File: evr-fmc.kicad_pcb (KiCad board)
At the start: 6 copper layers, 84 x 70.4 mm, 211 parts, among them J1 MMCX, J10 MMCX, J11 MMCX, J12 MMCX, J13 MMCX, J14 MMCX, J15 MMCX, J16 MMCX, J17 MMCX, J18 MMCX, J19 WP Jumper, J2 MMCX, J20 MMCX, J21 MMCX, J3 MMCX, J4 MMCX, J5 MMCX, J6 MMCX, J7 MMCX, J8 MMCX, J9 MMCX, P1 ASP-134488-01, Q1 FDN335N, Q2 FDN335N, T1 TCM2-43X, T2 TCM2-43X, T3 TCM2-43X, T4 TCM2-43X, U1 SN74LVC3G34DCT, U10 SN74LVC3G34DCT, U11 SN74LVC3G34DCT, U12 SN74LVC3G34DCT, U13 SN74LVC3G34DCT, U14 SN74LVC3G34DCT, U15 SN74LVC3G34DCT, U16 SN74LVC3G34DCT, U17 SN74LVC3G34DCT, U18 SI5394, U19 SI5394, U2 SN74LVC3G34DCT, U20 TLV75733PDBV, U21 TLV75718PDBV, U22 TPS562200, U23 74AVC4T245, U25 74AVC4T245, U26 74LVC8T245, U27 74LVC8T245, U3 SN74LVC3G34DCT, U4 SN74LVC3G34DCT, U5 SN74LVC3G34DCT, U6 SN74LVC3G34DCT, U7 SN74LVC3G34DCT, U8 SN74LVC3G34DCT, U9 AT24C64D, Y1 CX3225SB48000D0FPJC1, Y2 CX3225SB48000D0FPJC1

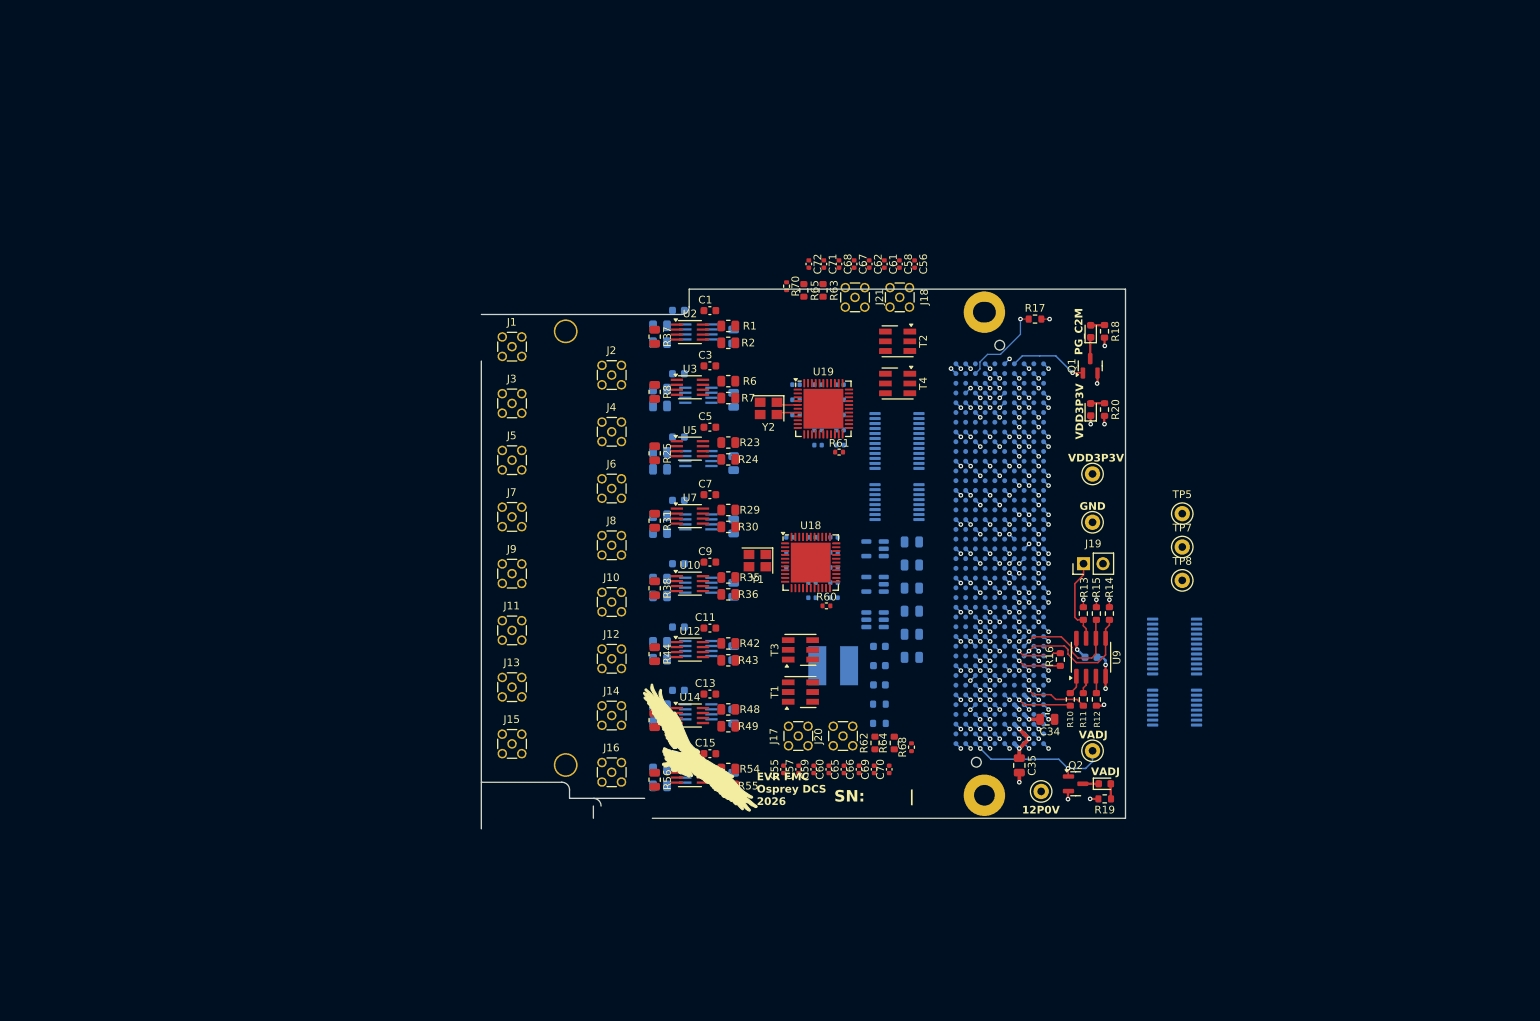
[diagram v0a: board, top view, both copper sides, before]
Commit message: Completed Schematic
Completed Schematic Draft
- Includes careful pin mapping to avoid conflicts with other firmwares
- Roughed out LCB layout high speed traces, and FMC breakouts.

Layout and BOM are still WIP
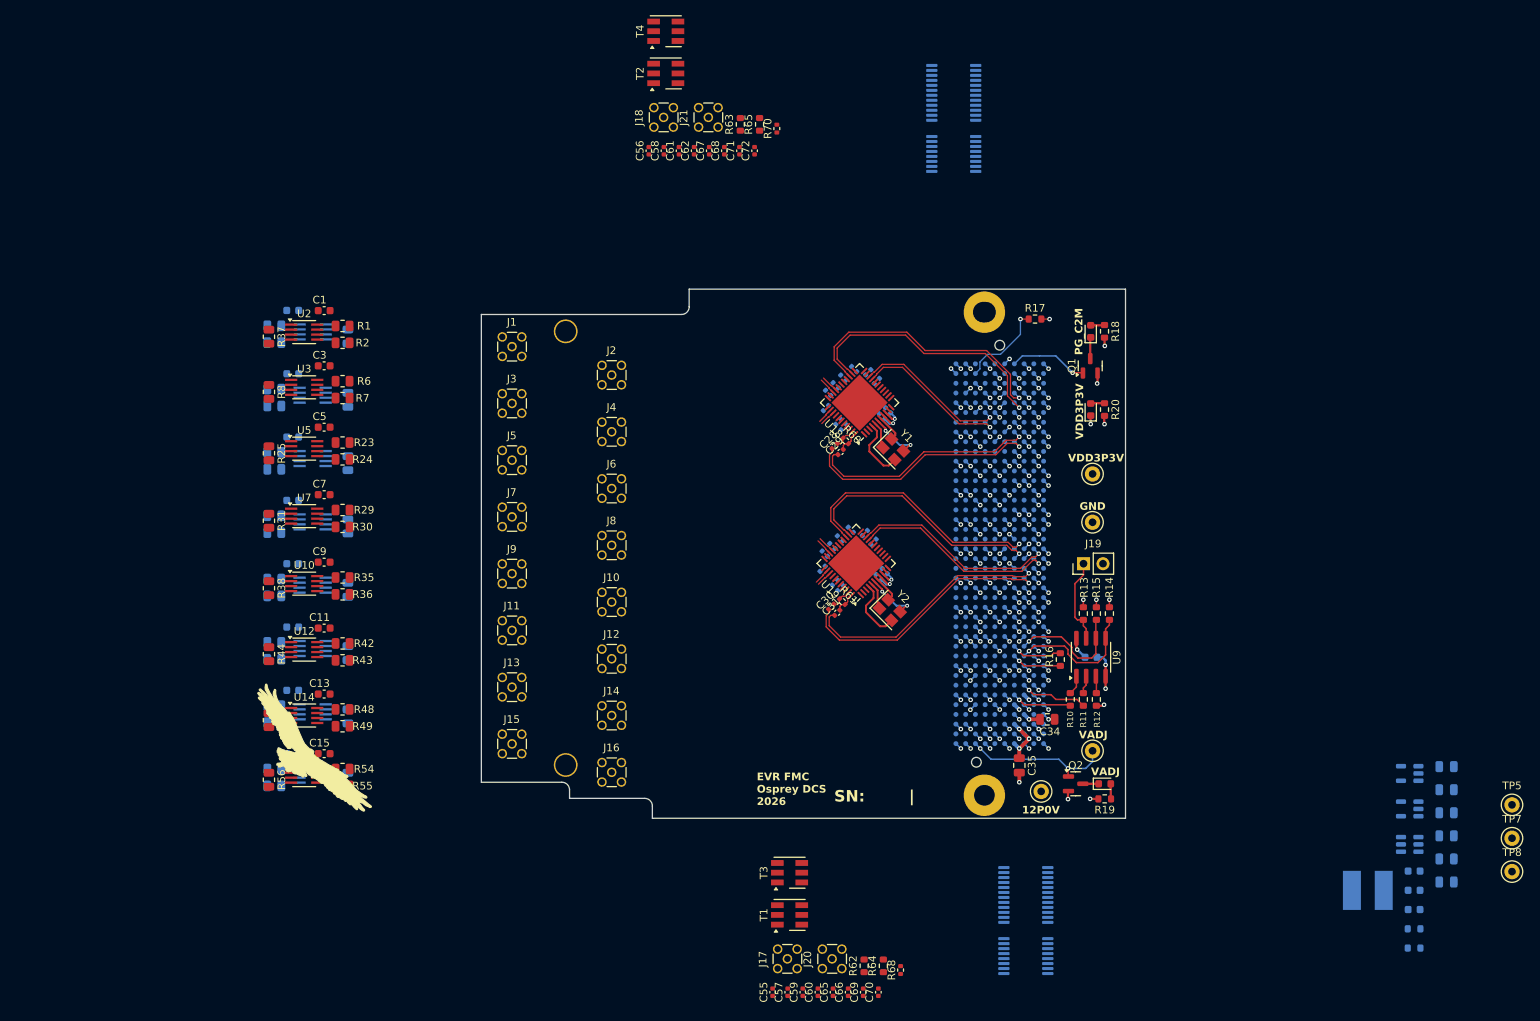
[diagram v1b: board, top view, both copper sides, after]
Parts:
- C28, C29, C30, C31: moved to F.Cu
- moved C48 75.6 mm to (232.9, 133.3)
- moved C49 75.6 mm to (232.9, 136.3)
- moved C50 75.6 mm to (232.9, 139.3)
- moved C51 75.6 mm to (232.9, 142.3)
- moved C53 75.6 mm to (232.9, 145.3)
- moved C54 75.6 mm to (232.9, 148.3)
- moved C46 75.6 mm to (228.6, 146.9)
- moved C47 75.6 mm to (228.6, 149.4)
- moved C52 75.6 mm to (228.6, 151.9)
- moved L1 75.6 mm to (222.6, 149.4)
- moved R66 75.6 mm to (228.6, 154.4)
- moved R67 75.6 mm to (228.6, 156.9)
- moved U20 75.6 mm to (228.1, 134.2)
- moved U21 75.6 mm to (228.1, 138.8)
- moved U22 75.6 mm to (228.1, 143.4)
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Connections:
- net Net-(U18-In0) renamed /Jitter Cleaner0/In0.P
- net Net-(U18-~{IN0}) renamed /Jitter Cleaner0/In0.N
- net Net-(U19-In0) renamed /Jitter Cleaner1/In0.P
- net Net-(U19-~{IN0}) renamed /Jitter Cleaner1/In0.N
- net P1_12P0V renamed +12V_FMC
- C28 pad 1: /FMC/FMC_CC_PAIR_0.P -> /FMC/Recovered_CLK_0.P
- C29 pad 1: /FMC/FMC_CC_PAIR_0.N -> /FMC/Recovered_CLK_0.N
- C30 pad 1: /FMC/FMC_CC_PAIR_1.P -> /FMC/Recovered_CLK_1.P
- C31 pad 1: /FMC/FMC_CC_PAIR_1.N -> /FMC/Recovered_CLK_1.N
- C47 pad 1: /Jitter Cleaner0/VDDA -> /Power/3P3V
- P1 pad C10: unconnected-(P1-PadC10) -> /FMC/Cleaner_SPI_0.CS
- P1 pad C11: unconnected-(P1-PadC11) -> /FMC/Cleaner_~{RST}_0
- P1 pad C14: unconnected-(P1-PadC14) -> /Digital IO/D_Output4
- P1 pad C15: unconnected-(P1-PadC15) -> /Digital IO/D_Output5
- P1 pad C18: unconnected-(P1-PadC18) -> /Digital IO/D_Output10
- P1 pad C19: unconnected-(P1-PadC19) -> /Digital IO/D_Output11
- P1 pad C22: unconnected-(P1-PadC22) -> /FMC/Recovered_CLK_1.N
- P1 pad C23: unconnected-(P1-PadC23) -> /FMC/Recovered_CLK_1.P
- P1 pad D12: unconnected-(P1-PadD12) -> /FMC/Cleaner_SPI_0.CLK
- P1 pad D14: unconnected-(P1-PadD14) -> /Digital IO/D_Output2
- P1 pad D15: unconnected-(P1-PadD15) -> /Digital IO/D_Output3
- P1 pad D17: unconnected-(P1-PadD17) -> /Digital IO/D_Output8
- P1 pad D18: unconnected-(P1-PadD18) -> /Digital IO/D_Output9
- P1 pad D20: unconnected-(P1-PadD20) -> /FMC/Cleaned_CLK_1.P
- P1 pad D21: unconnected-(P1-PadD21) -> /FMC/Cleaned_CLK_1.N
- P1 pad D24: unconnected-(P1-PadD24) -> /FMC/Cleaner_SPI_1.CLK
- P1 pad D26: unconnected-(P1-PadD26) -> /FMC/Cleaner_SPI_1.CS
- P1 pad D27: unconnected-(P1-PadD27) -> /FMC/Cleaner_~{RST}_1
- P1 pad D8: unconnected-(P1-PadD8) -> /FMC/Recovered_CLK_0.N
- P1 pad D9: unconnected-(P1-PadD9) -> /FMC/Recovered_CLK_0.P
- P1 pad G10: unconnected-(P1-PadG10) -> /FMC/Cleaner_SPI_0.DIN
- P1 pad G12: unconnected-(P1-PadG12) -> /Digital IO/D_Output0
- P1 pad G13: unconnected-(P1-PadG13) -> /Digital IO/D_Output1
- P1 pad G15: unconnected-(P1-PadG15) -> /Digital IO/D_Output6
- P1 pad G16: unconnected-(P1-PadG16) -> /Digital IO/D_Output7
- P1 pad G18: unconnected-(P1-PadG18) -> /Digital IO/D_Output12
- P1 pad G19: unconnected-(P1-PadG19) -> /Digital IO/D_Output13
- P1 pad G2: /FMC/FMC_CLK1_M2C.P -> unconnected-(P1-PadG2)
- P1 pad G21: unconnected-(P1-PadG21) -> /Digital IO/D_Output14
- P1 pad G22: unconnected-(P1-PadG22) -> /Digital IO/D_Output15
- P1 pad G24: unconnected-(P1-PadG24) -> /FMC/Cleaner_SPI_1.OE
- P1 pad G25: unconnected-(P1-PadG25) -> /FMC/Cleaner_SPI_1.DIN
- P1 pad G3: /FMC/FMC_CLK1_M2C.N -> unconnected-(P1-PadG3)
- P1 pad G6: unconnected-(P1-PadG6) -> /FMC/Cleaned_CLK_0.P
- P1 pad G7: unconnected-(P1-PadG7) -> /FMC/Cleaned_CLK_0.N
- P1 pad G9: unconnected-(P1-PadG9) -> /FMC/Cleaner_SPI_0.OE
- P1 pad H10: unconnected-(P1-PadH10) -> /FMC/Cleaner_Fault_0.LOL
- P1 pad H11: unconnected-(P1-PadH11) -> /FMC/Cleaner_SPI_0.DOUT
- P1 pad H25: unconnected-(P1-PadH25) -> /FMC/Cleaner_Fault_1.INTR
- P1 pad H26: unconnected-(P1-PadH26) -> /FMC/Cleaner_Fault_1.LOS_XO
- P1 pad H28: unconnected-(P1-PadH28) -> /FMC/Cleaner_Fault_1.LOL
- P1 pad H29: unconnected-(P1-PadH29) -> /FMC/Cleaner_SPI_1.DOUT
- P1 pad H4: /FMC/FMC_CLK0_M2C.P -> unconnected-(P1-PadH4)
- P1 pad H5: /FMC/FMC_CLK0_M2C.N -> unconnected-(P1-PadH5)
- P1 pad H7: unconnected-(P1-PadH7) -> /FMC/Cleaner_Fault_0.INTR
- P1 pad H8: unconnected-(P1-PadH8) -> /FMC/Cleaner_Fault_0.LOS_XO
- R10 pad 1: /EEPROM/GA1 -> /FMC/EEPROM_GA1
- R11 pad 1: /EEPROM/GA0 -> /FMC/EEPROM_GA0
- R14 pad 2: /EEPROM/SDA -> /FMC/EEPROM_SDA
- R15 pad 2: /EEPROM/SCL -> /FMC/EEPROM_SCL
- T1 pad 5: (no net) -> unconnected-(T1-OUT2-Pad5)
- T2 pad 5: (no net) -> unconnected-(T2-OUT2-Pad5)
- T3 pad 5: (no net) -> unconnected-(T3-OUT2-Pad5)
- T4 pad 5: (no net) -> unconnected-(T4-OUT2-Pad5)
- U18 pad 19: /FMC/FMC_GBTCLK0.N -> /FMC/Cleaned_CLK_0.N
- U18 pad 20: /FMC/FMC_GBTCLK0.P -> /FMC/Cleaned_CLK_0.P
- U18 pad 24: /FMC/FMC_CLK0_M2C.N -> /FMC/FMC_GBTCLK0.N
- U18 pad 25: /FMC/FMC_CLK0_M2C.P -> /FMC/FMC_GBTCLK0.P
- U19 pad 24: /FMC/FMC_CLK1_M2C.N -> /FMC/Cleaned_CLK_1.N
- U19 pad 25: /FMC/FMC_CLK1_M2C.P -> /FMC/Cleaned_CLK_1.P
- U21 pad 1: /Jitter Cleaner0/VDDA -> /Power/3P3V
- U21 pad 3: /Jitter Cleaner0/VDDA -> /Power/3P3V
- U23 pad 4: /Jitter Cleaner0/Cleaner_Fault.INTR -> /FMC/Cleaner_Fault_0.INTR
- U23 pad 5: /Jitter Cleaner0/Cleaner_Fault.LOS_XO -> /FMC/Cleaner_Fault_0.LOS_XO
- U23 pad 6: /Jitter Cleaner0/Cleaner_Fault.LOL -> /FMC/Cleaner_Fault_0.LOL
- U23 pad 7: /Jitter Cleaner0/Cleaner_SPI.DOUT -> /FMC/Cleaner_SPI_0.DOUT
- U25 pad 4: /Jitter Cleaner1/Cleaner_Fault.INTR -> /FMC/Cleaner_Fault_1.INTR
- U25 pad 5: /Jitter Cleaner1/Cleaner_Fault.LOS_XO -> /FMC/Cleaner_Fault_1.LOS_XO
- U25 pad 6: /Jitter Cleaner1/Cleaner_Fault.LOL -> /FMC/Cleaner_Fault_1.LOL
- U25 pad 7: /Jitter Cleaner1/Cleaner_SPI.DOUT -> /FMC/Cleaner_SPI_1.DOUT
- U26 pad 3: /Jitter Cleaner0/Cleaner_SPI.OE -> /FMC/Cleaner_SPI_0.OE
- U26 pad 4: /Jitter Cleaner0/Cleaner_SPI.DIN -> /FMC/Cleaner_SPI_0.DIN
- U26 pad 5: /Jitter Cleaner0/Cleaner_SPI.CLK -> /FMC/Cleaner_SPI_0.CLK
- U26 pad 7: /Jitter Cleaner0/Cleaner_SPI.CS -> /FMC/Cleaner_SPI_0.CS
- U26 pad 8: /Jitter Cleaner0/~{RST} -> /FMC/Cleaner_~{RST}_0
- U27 pad 3: /Jitter Cleaner1/Cleaner_SPI.OE -> /FMC/Cleaner_SPI_1.OE
- U27 pad 4: /Jitter Cleaner1/Cleaner_SPI.DIN -> /FMC/Cleaner_SPI_1.DIN
- U27 pad 5: /Jitter Cleaner1/Cleaner_SPI.CLK -> /FMC/Cleaner_SPI_1.CLK
- U27 pad 7: /Jitter Cleaner1/Cleaner_SPI.CS -> /FMC/Cleaner_SPI_1.CS
- U27 pad 8: /Jitter Cleaner1/~{RST} -> /FMC/Cleaner_~{RST}_1
- U9 pad 5: /EEPROM/SDA -> /FMC/EEPROM_SDA
- U9 pad 6: /EEPROM/SCL -> /FMC/EEPROM_SCL
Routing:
- net /FMC/FMC_GBTCLK0.P: track 0.91 -> 35.6 mm
- net /FMC/FMC_GBTCLK0.N: track 0.91 -> 35.0 mm
- net /FMC/Cleaned_CLK_1.P: track 0.00 -> 34.1 mm, vias 0 -> 1
- net /FMC/Recovered_CLK_1.P: track 0.00 -> 34.0 mm, vias 0 -> 1
- net /FMC/Cleaned_CLK_1.N: track 0.00 -> 33.1 mm, vias 0 -> 1
- net /FMC/Recovered_CLK_1.N: track 0.00 -> 33.1 mm, vias 0 -> 1
- net /FMC/Recovered_CLK_0.P: track 0.00 -> 30.9 mm, vias 0 -> 1
- net /FMC/Recovered_CLK_0.N: track 0.00 -> 29.9 mm, vias 0 -> 1
- net /FMC/FMC_GBTCLK1.P: track 0.91 -> 27.2 mm
- net /FMC/FMC_GBTCLK1.N: track 0.91 -> 26.9 mm
- net /FMC/Cleaned_CLK_0.P: track 0.00 -> 20.5 mm, vias 0 -> 1
- net /FMC/Cleaned_CLK_0.N: track 0.00 -> 20.2 mm, vias 0 -> 1
- net /Jitter Cleaner0/VDDA: track 0.00 -> 11.3 mm, vias 0 -> 4
- net Net-(U18-X1): track 0.00 -> 8.37 mm
- net Net-(U19-X1): track 0.00 -> 8.37 mm
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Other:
- board size 84 x 70.4 mm -> 84 x 69 mm

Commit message: Updated Schematic and continued layout work
schematic:
- Added 0ohm resistor in power section
- Added pull up and down to digital lines to define powerup behavior
- Added some power filter between jitter cleaner IC's

layout:
-Overall Still WIP
-defined all needed fmc pins
-started layout of critical clock signals and connector locations.
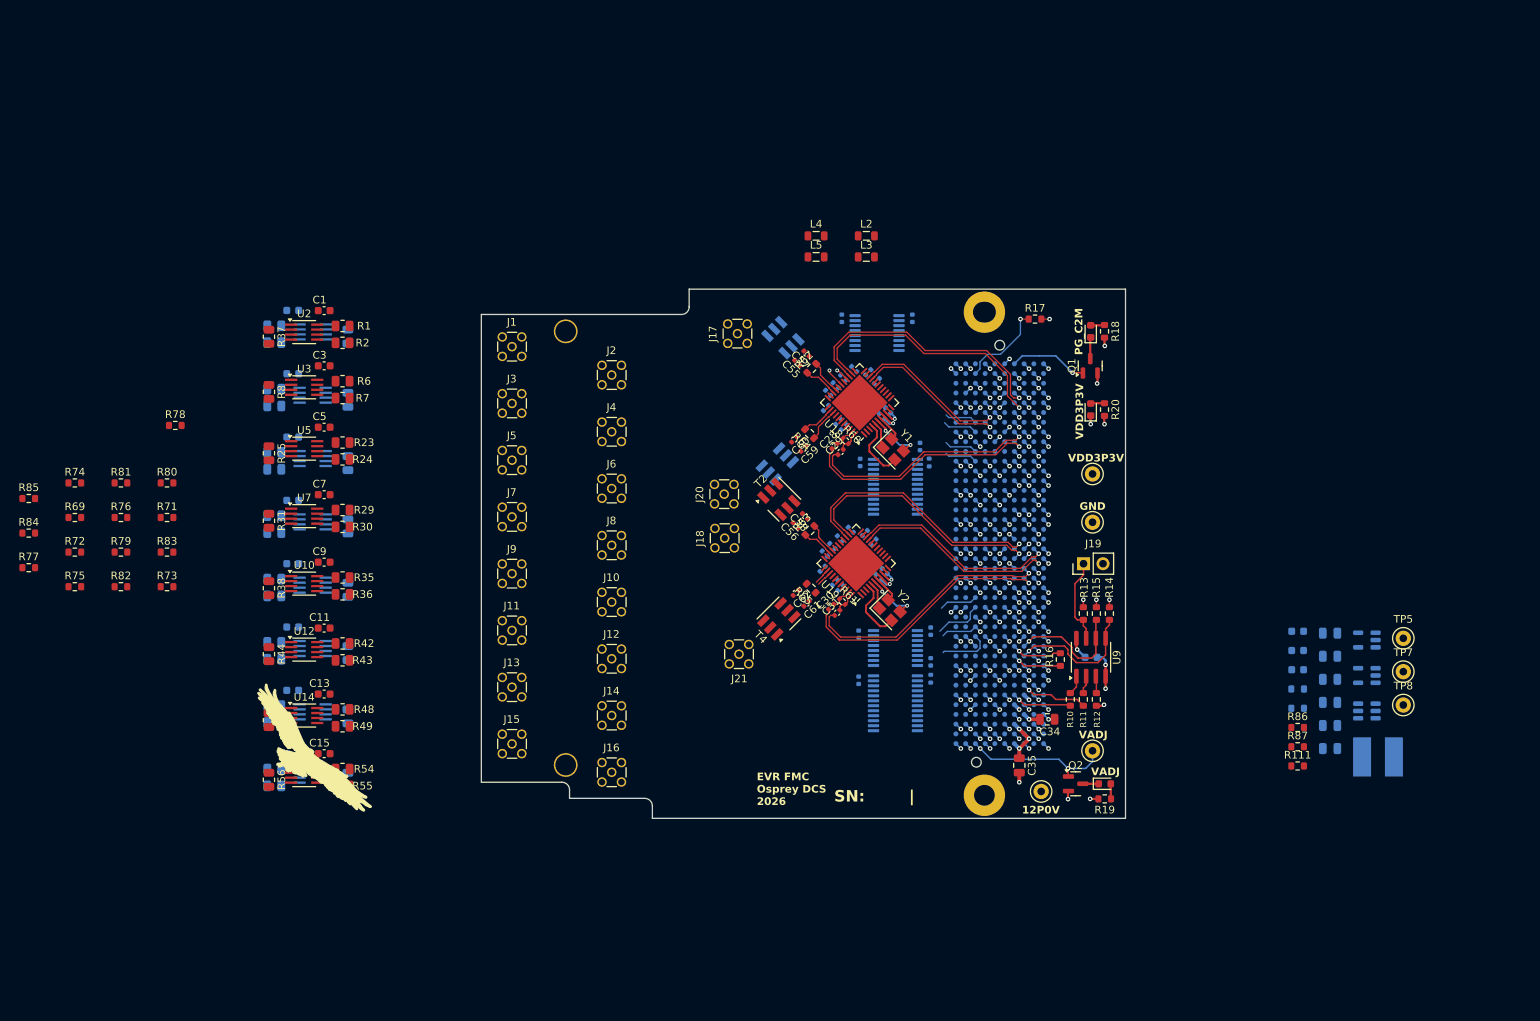
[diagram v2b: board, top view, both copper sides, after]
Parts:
- added L2: 60R@100Mhz; 3.5A, Inductor_SMD:L_0805_2012Metric, F.Cu at (157.2, 64.0)
- added L3: 60R@100Mhz; 3.5A, Inductor_SMD:L_0805_2012Metric, F.Cu at (157.2, 66.8)
- added L4: 60R@100Mhz; 3.5A, Inductor_SMD:L_0805_2012Metric, F.Cu at (150.7, 64.0)
- added L5: 60R@100Mhz; 3.5A, Inductor_SMD:L_0805_2012Metric, F.Cu at (150.7, 66.8)
- added R111: 0R, Resistor_SMD:R_0603_1608Metric, F.Cu at (213.4, 133.2)
- added R69: 11.5k, Resistor_SMD:R_0603_1608Metric, F.Cu at (54.0, 100.8)
- added R71: 11.5k, Resistor_SMD:R_0603_1608Metric, F.Cu at (66.0, 100.8)
- added R72: 11.5k, Resistor_SMD:R_0603_1608Metric, F.Cu at (54.0, 105.3)
- added R73: 11.5k, Resistor_SMD:R_0603_1608Metric, F.Cu at (66.0, 109.8)
- added R74: 11.5k, Resistor_SMD:R_0603_1608Metric, F.Cu at (54.0, 96.3)
- added R75: 11.5k, Resistor_SMD:R_0603_1608Metric, F.Cu at (54.0, 109.8)
- added R76: 11.5k, Resistor_SMD:R_0603_1608Metric, F.Cu at (60.0, 100.8)
- added R77: 11.5k, Resistor_SMD:R_0603_1608Metric, F.Cu at (48.0, 107.3)
- added R78: 11.5k, Resistor_SMD:R_0603_1608Metric, F.Cu at (67.1, 88.8)
- added R79: 11.5k, Resistor_SMD:R_0603_1608Metric, F.Cu at (60.0, 105.3)
- added R80: 11.5k, Resistor_SMD:R_0603_1608Metric, F.Cu at (66.0, 96.3)
- added R81: 11.5k, Resistor_SMD:R_0603_1608Metric, F.Cu at (60.0, 96.3)
- added R82: 11.5k, Resistor_SMD:R_0603_1608Metric, F.Cu at (60.0, 109.8)
- added R83: 11.5k, Resistor_SMD:R_0603_1608Metric, F.Cu at (66.0, 105.3)
- added R84: 11.5k, Resistor_SMD:R_0603_1608Metric, F.Cu at (48.0, 102.8)
- added R85: 11.5k, Resistor_SMD:R_0603_1608Metric, F.Cu at (48.0, 98.3)
- added R86: 0R, Resistor_SMD:R_0603_1608Metric, F.Cu at (213.4, 128.2)
- added R87: 0R, Resistor_SMD:R_0603_1608Metric, F.Cu at (213.4, 130.7)
- C65, C66, C67, C68, C69, C70, C71, C72, R68, R70: moved to B.Cu
- T1, T3: value TCM2-43X -> TCM2-43X+; moved to B.Cu
- T2, T4: value TCM2-43X -> TCM2-43X+
- moved C66 88.3 mm to (163.2, 74.8)
- moved C65 87.9 mm to (154.0, 74.8)
- moved C57 83.3 mm to (149.4, 79.4), turned to 135 degrees
- moved C55 82.1 mm to (148.2, 80.6), turned to 135 degrees
- moved J17 81.8 mm to (140.4, 76.8)
- moved R62 78.2 mm to (150.1, 81.3), turned to 45 degrees
- moved T4 78.0 mm to (145.8, 114.0), turned to 135 degrees
- moved T1 75.3 mm to (146.3, 77.3), turned to -135 degrees
- moved R70 74.5 mm to (165.6, 121.8)
- moved C60 72.1 mm to (147.8, 90.6), turned to -135 degrees
- moved C69 71.5 mm to (164.2, 91.5), turned to -90 degrees
- moved C71 71.2 mm to (165.6, 119.6), turned to -90 degrees
- moved C59 70.9 mm to (149.0, 91.8), turned to -135 degrees
- moved C72 70.4 mm to (156.2, 122.0)
- moved J21 70.1 mm to (140.6, 118.6), turned to 180 degrees
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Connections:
- net /FMC/Cleaner_SPI_0.DIN renamed /FMC/Cleaner_SPI_0.SDI
- net /FMC/Cleaner_SPI_0.DOUT renamed /FMC/Cleaner_SPI_0.SDO
- net /FMC/Cleaner_SPI_1.DIN renamed /FMC/Cleaner_SPI_1.SDI
- net /FMC/Cleaner_SPI_1.DOUT renamed /FMC/Cleaner_SPI_1.SDO
- net /Jitter Cleaner0/SPI_DIN renamed /Jitter Cleaner0/SPI_SDI
- net /Jitter Cleaner0/SPI_DOUT renamed /Jitter Cleaner0/SPI_SDO
- net /Jitter Cleaner1/SPI_DIN renamed /Jitter Cleaner1/SPI_SDI
- net /Jitter Cleaner1/SPI_DOUT renamed /Jitter Cleaner1/SPI_SDO
- C17 pad 1: /Jitter Cleaner0/VDDA -> Net-(C17-Pad1)
- C18 pad 1: /Jitter Cleaner0/VDDA -> Net-(C17-Pad1)
- C23 pad 1: /Jitter Cleaner0/VDD -> Net-(C23-Pad1)
- C24 pad 1: /Jitter Cleaner0/VDD -> Net-(C23-Pad1)
- C25 pad 1: /Jitter Cleaner0/VDD -> Net-(C23-Pad1)
- C26 pad 1: /Jitter Cleaner0/VDD -> Net-(C23-Pad1)
- C27 pad 1: /Jitter Cleaner0/VDDA -> VDD3P3V
- C37 pad 1: /Jitter Cleaner0/VDDA -> Net-(C37-Pad1)
- C39 pad 1: /Jitter Cleaner0/VDDA -> Net-(C37-Pad1)
- C41 pad 1: /Jitter Cleaner0/VDD -> Net-(C41-Pad1)
- C42 pad 1: /Jitter Cleaner0/VDDA -> VDD3P3V
- C43 pad 1: /Jitter Cleaner0/VDD -> Net-(C41-Pad1)
- C44 pad 1: /Jitter Cleaner0/VDD -> Net-(C41-Pad1)
- C45 pad 1: /Jitter Cleaner0/VDD -> Net-(C41-Pad1)
- C50 pad 1: /Jitter Cleaner0/VDDA -> Net-(U20-OUT)
- C51 pad 1: /Jitter Cleaner0/VDD -> Net-(U21-OUT)
- C53 pad 1: /Power/4P3V -> Net-(C53-Pad1)
- C54 pad 1: /Power/4P3V -> Net-(C53-Pad1)
- C65 pad 2: /Jitter Cleaner0/VDDA -> VDD3P3V
- C67 pad 2: /Jitter Cleaner0/VDDA -> VDD3P3V
- C70 pad 2: /Jitter Cleaner0/VDDA -> VDD3P3V
- C72 pad 2: /Jitter Cleaner0/VDDA -> VDD3P3V
- L1 pad 2: /Power/4P3V -> Net-(C53-Pad1)
- R66 pad 1: /Power/4P3V -> Net-(C53-Pad1)
- TP5 pad 1: /Jitter Cleaner0/VDD -> Net-(U21-OUT)
- TP7 pad 1: /Jitter Cleaner0/VDDA -> Net-(U20-OUT)
- TP8 pad 1: /Power/4P3V -> Net-(C53-Pad1)
- U18 pad 21: /Jitter Cleaner0/VDD -> Net-(C23-Pad1)
- U18 pad 26: /Jitter Cleaner0/VDDA -> VDD3P3V
- U18 pad 32: /Jitter Cleaner0/VDD -> Net-(C23-Pad1)
- U18 pad 39: /Jitter Cleaner0/VDD -> Net-(C23-Pad1)
- U18 pad 40: /Jitter Cleaner0/VDD -> Net-(C23-Pad1)
- U18 pad 8: /Jitter Cleaner0/VDDA -> Net-(C17-Pad1)
- U18 pad 9: /Jitter Cleaner0/VDDA -> Net-(C17-Pad1)
- U19 pad 21: /Jitter Cleaner0/VDD -> Net-(C41-Pad1)
- U19 pad 26: /Jitter Cleaner0/VDDA -> VDD3P3V
- U19 pad 32: /Jitter Cleaner0/VDD -> Net-(C41-Pad1)
- U19 pad 39: /Jitter Cleaner0/VDD -> Net-(C41-Pad1)
- U19 pad 40: /Jitter Cleaner0/VDD -> Net-(C41-Pad1)
- U19 pad 8: /Jitter Cleaner0/VDDA -> Net-(C37-Pad1)
- U19 pad 9: /Jitter Cleaner0/VDDA -> Net-(C37-Pad1)
- U20 pad 5: /Jitter Cleaner0/VDDA -> Net-(U20-OUT)
- U21 pad 5: /Jitter Cleaner0/VDD -> Net-(U21-OUT)
- U23 pad 16: /Jitter Cleaner0/VDDA -> VDD3P3V
- U25 pad 16: /Jitter Cleaner0/VDDA -> VDD3P3V
- U26 pad 23: /Jitter Cleaner0/VDDA -> VDD3P3V
- U26 pad 24: /Jitter Cleaner0/VDDA -> VDD3P3V
- U27 pad 23: /Jitter Cleaner0/VDDA -> VDD3P3V
- U27 pad 24: /Jitter Cleaner0/VDDA -> VDD3P3V
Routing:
- net /Jitter Cleaner0/VDDA: track 11.3 -> 0.00 mm, vias 4 -> 0
- net /FMC/Cleaner_Fault_1.LOS_XO: track 0.00 -> 6.44 mm
- net /FMC/Cleaner_SPI_1.SDO: track 0.91 -> 6.85 mm, vias 1 -> 0
- net Net-(C17-Pad1): track 0.00 -> 5.67 mm, vias 0 -> 2
- net Net-(C37-Pad1): track 0.00 -> 5.67 mm, vias 0 -> 2
- net /FMC/Cleaner_Fault_1.INTR: track 0.00 -> 5.00 mm
- net /FMC/Cleaner_Fault_1.LOL: track 0.91 -> 5.62 mm
- net /FMC/Cleaner_Fault_0.LOS_XO: track 0.00 -> 4.53 mm
- net /FMC/Cleaner_Fault_0.LOL: track 0.00 -> 4.31 mm
- net /FMC/Cleaner_SPI_0.SDO: track 0.00 -> 4.25 mm
- net /FMC/Cleaner_Fault_0.INTR: track 0.00 -> 4.22 mm
- net /Jitter Cleaner0/LOS_XO: track 0.00 -> 2.49 mm, vias 0 -> 1
- net /Jitter Cleaner0/Cleaned_CLK3.N: track 2.09 -> 4.42 mm
- net /Jitter Cleaner0/Cleaned_CLK3.P: track 2.09 -> 4.42 mm
- net /Jitter Cleaner0/Cleaned_CLK2.N: track 2.29 -> 4.53 mm
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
